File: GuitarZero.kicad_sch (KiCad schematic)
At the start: 2 parts, among them J1 AudioJack2_Ground, J2 USB_B_Micro

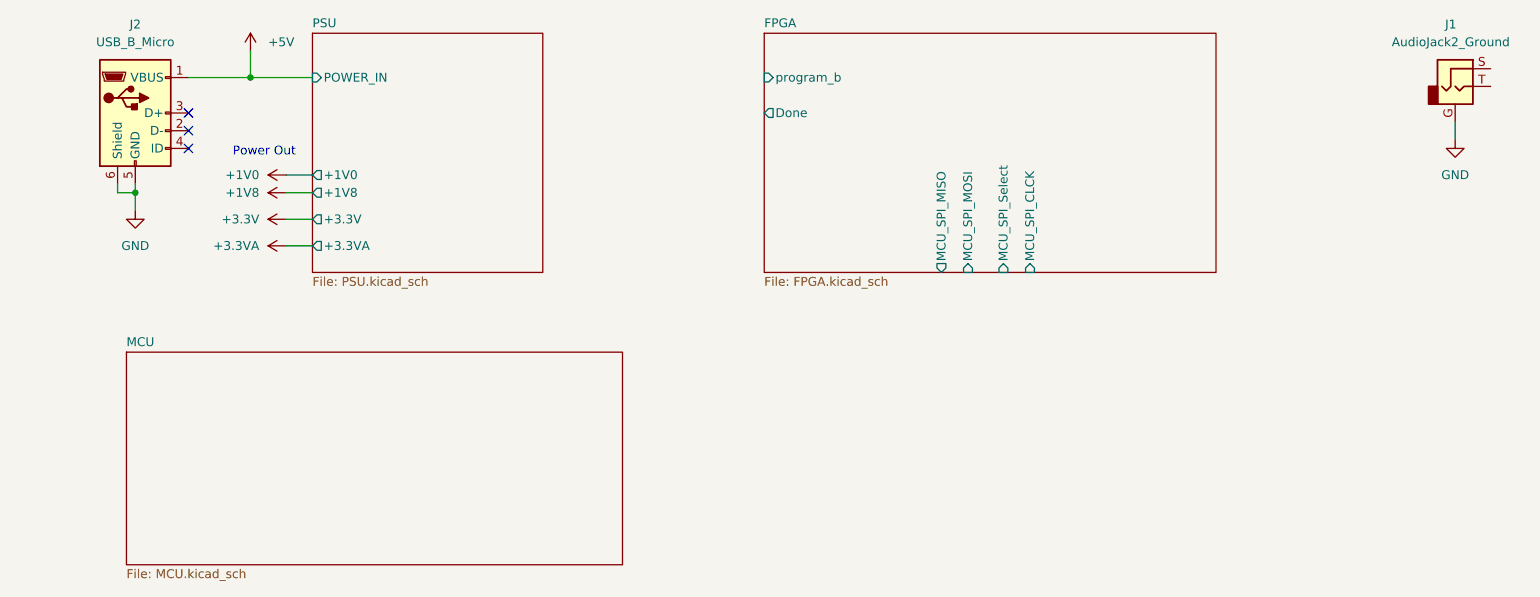
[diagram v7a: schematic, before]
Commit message: Connected MCU and FPGA via SPI
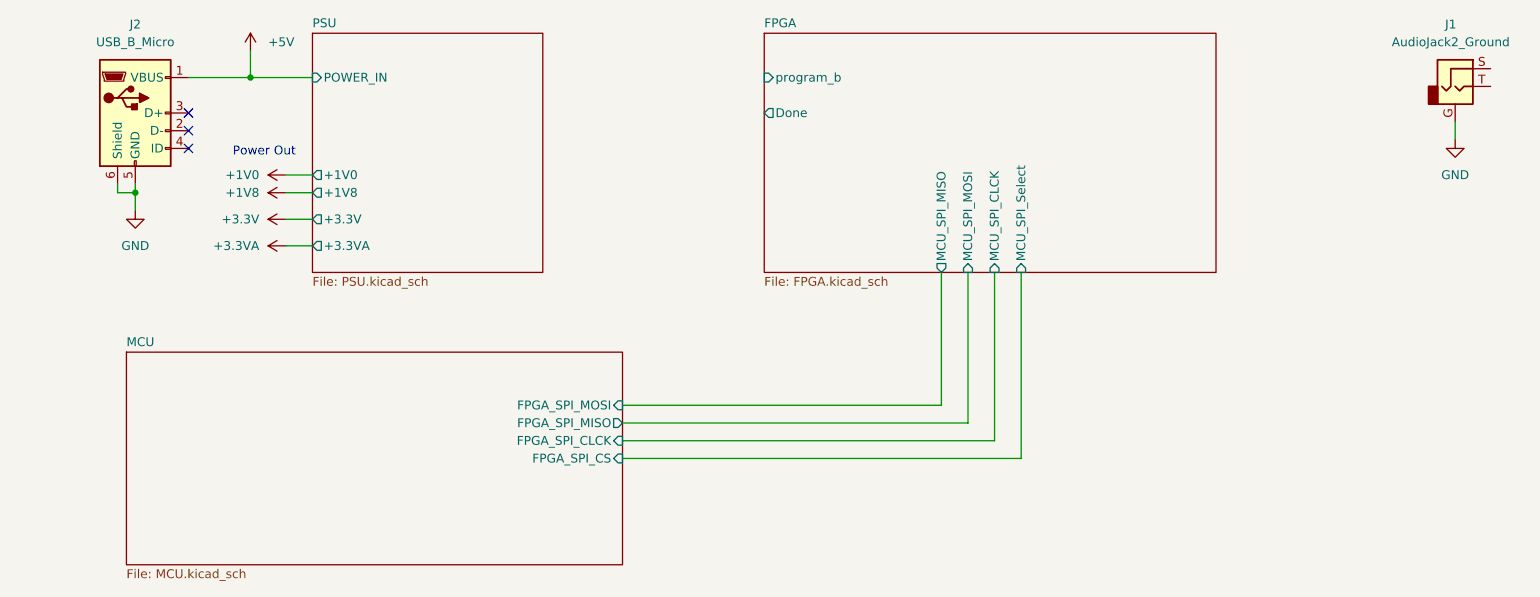
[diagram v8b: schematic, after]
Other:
- sheet MCU ports: added FPGA_SPI_CLCK, FPGA_SPI_CS, FPGA_SPI_MISO, FPGA_SPI_MOSI; removed none
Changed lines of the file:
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@@
+    (stroke (width 0) (type default))
+  )
+  (wire (pts (xy 157.48 59.69) (xy 157.48 86.36))
     (stroke (width 0) (type default))
   )
@@
     (stroke (width 0) (type default))
   )
+  (wire (pts (xy 157.48 86.36) (xy 100.33 86.36))
+    (stroke (width 0) (type default))
+  )
   (wire (pts (xy 52.07 55.88) (xy 55.88 55.88))
     (stroke (width 0) (type default))
   )
+  (wire (pts (xy 146.05 59.69) (xy 146.05 78.74))
+    (stroke (width 0) (type default))
+  )
   (wire (pts (xy 46.99 31.75) (xy 55.88 31.75))
     (stroke (width 0) (type default))
   )
+  (wire (pts (xy 153.67 59.69) (xy 153.67 83.82))
+    (stroke (width 0) (type default))
+  )
   (wire (pts (xy 46.99 31.75) (xy 46.99 27.94))
     (stroke (width 0) (type default))
@@
     (stroke (width 0) (type default))
   )
+  (wire (pts (xy 100.33 78.74) (xy 146.05 78.74))
+    (stroke (width 0) (type default))
+  )
   (wire (pts (xy 52.07 48.26) (xy 55.88 48.26))
     (stroke (width 0) (type default))
@@
   )
   (wire (pts (xy 52.07 45.72) (xy 55.88 45.72))
+    (stroke (width 0) (type default))
+  )
+  (wire (pts (xy 149.86 81.28) (xy 149.86 59.69))
+    (stroke (width 0) (type default))
+  )
+  (wire (pts (xy 100.33 81.28) (xy 149.86 81.28))
+    (stroke (width 0) (type default))
+  )
+  (wire (pts (xy 153.67 83.82) (xy 100.33 83.82))
     (stroke (width 0) (type default))
   )
@@
       (effects (font (size 1.27 1.27)) (justify left))
     )
-    (pin "MCU_SPI_Select" input (at 154.94 59.69 270)
-      (effects (font (size 1.27 1.27)) (justify left))
-    )
-    (pin "MCU_SPI_CLCK" input (at 158.75 59.69 270)
+    (pin "MCU_SPI_Select" input (at 157.48 59.69 270)
+      (effects (font (size 1.27 1.27)) (justify left))
+    )
+    (pin "MCU_SPI_CLCK" input (at 153.67 59.69 270)
       (effects (font (size 1.27 1.27)) (justify left))
     )
@@
       (effects (font (size 1.27 1.27)) (justify left top))
     )
-    (instances
+    (pin "FPGA_SPI_MOSI" input (at 100.33 78.74 0)
+      (effects (font (size 1.27 1.27)) (justify right))
+    )
+    (pin "FPGA_SPI_CS" input (at 100.33 86.36 0)
+      (effects (font (size 1.27 1.27)) (justify right))
+    )
+    (pin "FPGA_SPI_CLCK" input (at 100.33 83.82 0)
+      (effects (font (size 1.27 1.27)) (justify right))
+    )
+    (pin "FPGA_SPI_MISO" output (at 100.33 81.28 0)
+      (effects (font (size 1.27 1.27)) (justify right))
+    )
+    (instances
